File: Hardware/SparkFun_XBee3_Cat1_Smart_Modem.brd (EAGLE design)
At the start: 45.7 x 54.6 mm, 129 parts, among them J4 QWIIC_RIGHT_ANGLE, Q2 3.1A/30V/105mΩ, U1 FSUSB30MUX_MSOP10, U2 AP63203, U3 ESD Diode, U5 ESD Diode, U6 CP210X

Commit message: Updates xbee sybmol to include pin numbers
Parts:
- J2: device xbee_improved:XBEE-SMD_SILK -> xbee_smart_modem:XBEE-SMD_SILK
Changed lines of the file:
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@@
 <drawing>
 <settings>
-<setting alwaysvectorfont="no"/>
+<setting alwaysvectorfont="yes"/>
 <setting verticaltext="up"/>
 </settings>
@@
 <layers>
 <layer number="1" name="Top" color="4" fill="1" visible="yes" active="yes"/>
-<layer number="2" name="Route2" color="23" fill="1" visible="yes" active="yes"/>
-<layer number="15" name="Route15" color="39" fill="1" visible="yes" active="yes"/>
+<layer number="2" name="Route2" color="23" fill="1" visible="no" active="yes"/>
+<layer number="15" name="Route15" color="39" fill="1" visible="no" active="yes"/>
 <layer number="16" name="Bottom" color="3" fill="1" visible="yes" active="yes"/>
 <layer number="17" name="Pads" color="26" fill="1" visible="yes" active="yes"/>
@@
 <layer number="115" name="ReferenceISLANDS" color="7" fill="1" visible="no" active="yes"/>
 <layer number="116" name="Patch_BOT" color="9" fill="4" visible="no" active="yes"/>
-<layer number="117" name="PM_Ref" color="26" fill="1" visible="no" active="yes"/>
+<layer number="117" name="PM_Ref" color="26" fill="1" visible="yes" active="yes"/>
 <layer number="118" name="Rect_Pads" color="7" fill="1" visible="no" active="yes"/>
-<layer number="119" name="PF_Ref" color="31" fill="1" visible="no" active="yes"/>
-<layer number="120" name="WFL_Ref" color="25" fill="1" visible="no" active="yes"/>
+<layer number="119" name="PF_Ref" color="31" fill="1" visible="yes" active="yes"/>
+<layer number="120" name="WFL_Ref" color="25" fill="1" visible="yes" active="yes"/>
 <layer number="121" name="_tsilk" color="7" fill="1" visible="no" active="yes"/>
 <layer number="122" name="_bsilk" color="7" fill="1" visible="no" active="yes"/>
@@
 <attribute name="VALUE" x="33.02" y="7.62" size="0.6096" layer="27" font="vector" ratio="20" align="bottom-center"/>
 </element>
-<element name="J2" library="xbee_improved" package="XBEE-SMD_SILK" value="" x="22.86" y="33.02" smashed="yes">
+<element name="J2" library="xbee_smart_modem" package="XBEE-SMD_SILK" value="" x="22.86" y="33.02" smashed="yes">
 <attribute name="NAME" x="22.86" y="33.29" size="0.6096" layer="25" font="vector" ratio="20" align="bottom-center"/>
+<attribute name="PROD_ID" value="WRL-17581" x="22.86" y="33.02" size="1.778" layer="27" display="off"/>
 <attribute name="VALUE" x="22.86" y="32.75" size="0.6096" layer="27" font="vector" ratio="20" align="top-center"/>
 </element>
@@
 </signals>
 <mfgpreviewcolors>
-<mfgpreviewcolor name="soldermaskcolor" color="0xC8AA0000"/>
+<mfgpreviewcolor name="soldermaskcolor" color="0xC8000000"/>
 <mfgpreviewcolor name="silkscreencolor" color="0xFFFEFEFE"/>
 <mfgpreviewcolor name="backgroundcolor" color="0xFF282828"/>

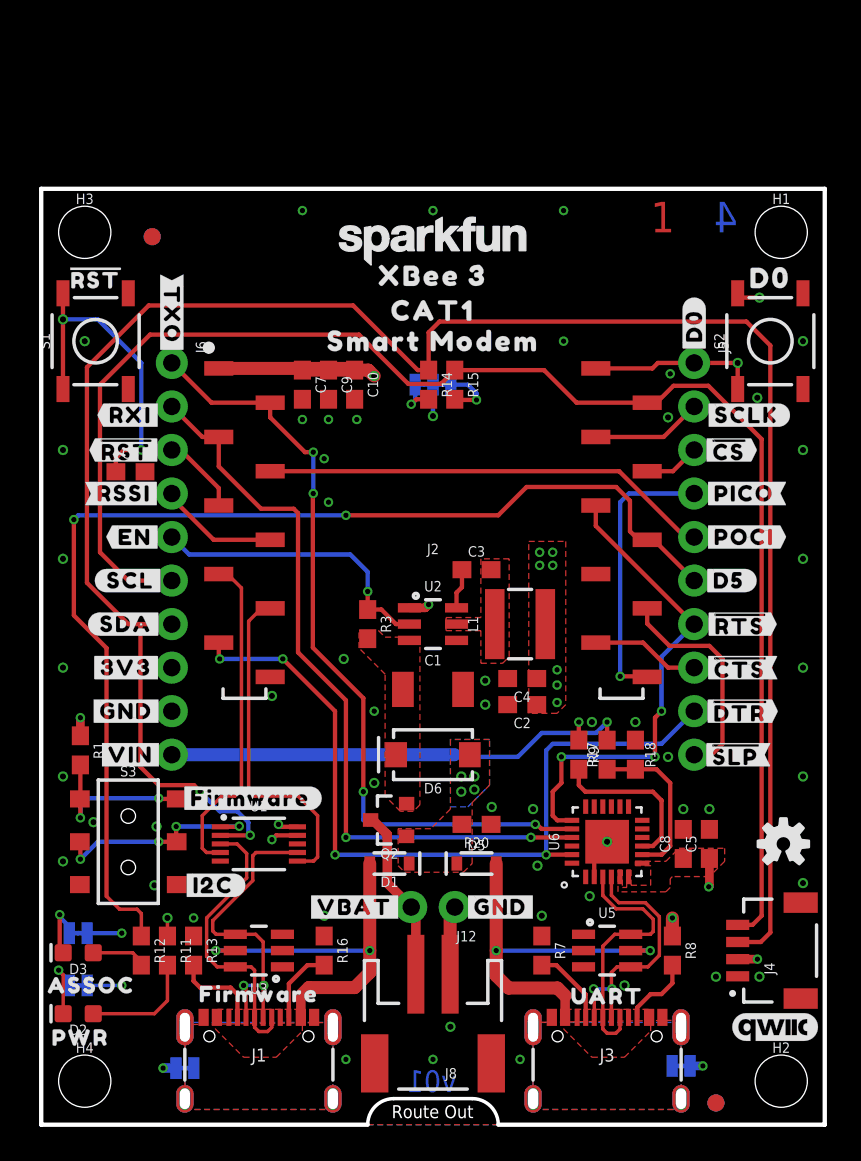
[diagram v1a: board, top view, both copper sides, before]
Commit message: Updates library to include a version of the module with silk
* Replaces module in design with the silk-ed version
* Extends board to be able to include the module's outline in silk
* Moves buttons and through holes to fit new size
* Changes name of the product to "Xbee 3 Dev Kit"
* Moves switch to make space for new silk
* Adds RSSI LED
* Rolls version to v02
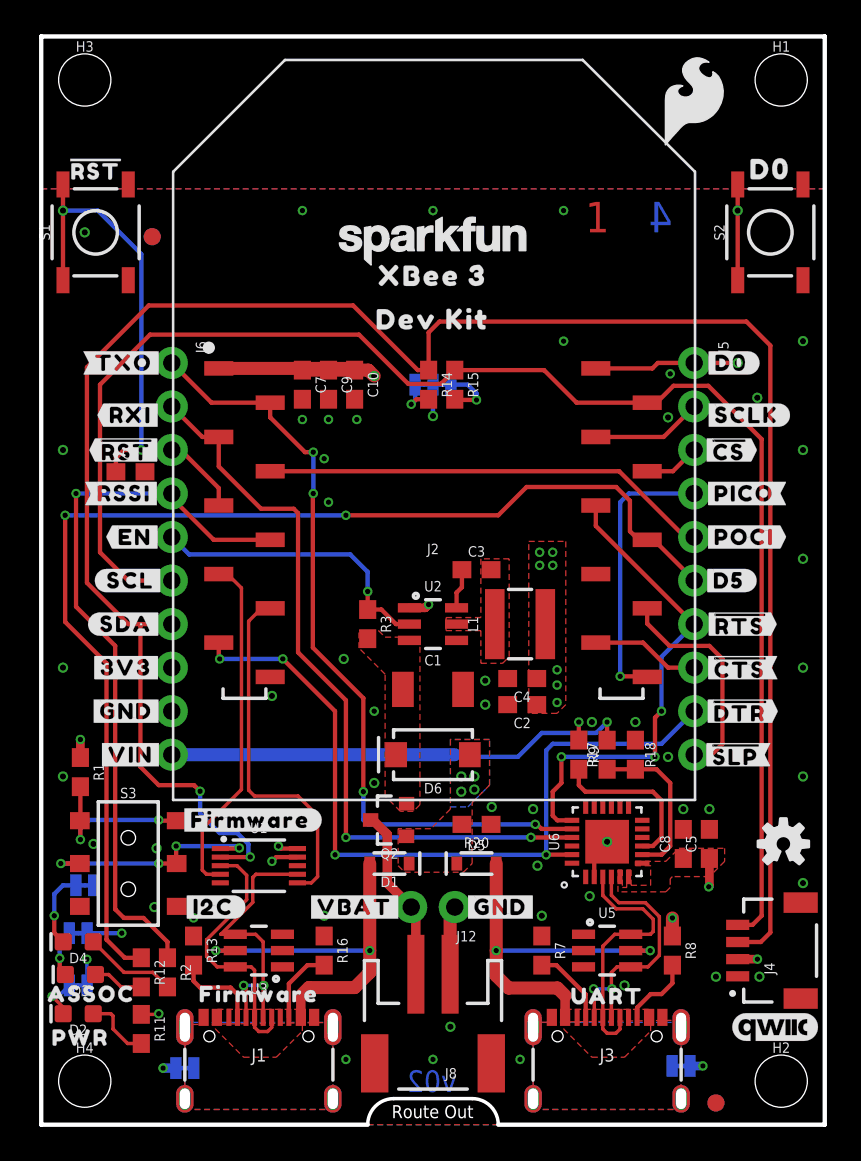
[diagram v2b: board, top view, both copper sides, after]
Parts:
- removed U$62: (no value), top:SMART1337
- removed U$64: (no value), top:MODEM1338
- added D4: BLUE, SparkFun-LED:LED-0603
- added R2: 2.2k, SparkFun-Resistors:0603
- added RLED: JUMPER-SMT_2_NC_TRACE_SILK, SparkFun-Jumpers:SMT-JUMPER_2_NC_TRACE_SILK
- J2: device xbee_smart_modem:XBEE-SMD_SILK -> xbee_smart_modem:XBEE3-SMD_SILK
- U$51: device top:SMART_MODEM1337 -> top:DEV_KIT1340
- U$52: device top:CAT1336 -> top:DEV_KIT1340
- U$61: device top:CAT1336 -> SparkFun-Aesthetics:SFE_LOGO_FLAME_.2
- moved U$61 27.5 mm to (38.1, 59.7), flipped to the top
- moved U$52 10.7 mm to (22.9, 36.8), flipped to the bottom
- moved H1 8.89 mm to (43.2, 61.0)
- moved H3 8.89 mm to (2.54, 61.0)
- moved S1 6.35 mm to (3.17, 52.1)
- moved S2 6.35 mm to (42.5, 52.1)
- moved U$30 6.35 mm to (3.17, 55.8)
- moved U$40 6.35 mm to (42.5, 55.8)
- moved R11 4.82 mm to (5.84, 5.59)
- moved U$50 3.95 mm to (4.83, 44.5), turned to 0 degrees
- moved U$10 3.05 mm to (40.3, 44.5), turned to 0 degrees
- moved D3 1.28 mm to (2.29, 8.76)
- moved U$51 1.27 mm to (22.9, 47.0)
- moved S3 1.27 mm to (5.08, 15.2)
- moved U$49 1.27 mm to (10.0, 12.7)
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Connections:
- net N$3 renamed FIRMWARE
- new net N$2: D4.A, R2.2
- new net N$3: D4.C, RLED.2
- net D10/RSSI_PWM: now also R2.1
- net GND: now also RLED.1
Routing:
- net D10/RSSI_PWM: track 7.01 -> 42.6 mm, vias 0 -> 1
- net D0: track 15.8 -> 22.9 mm
- net !RESET!: track 25.2 -> 31.6 mm
- net N$2: track 0.00 -> 5.42 mm
- net N$3: track 0.00 -> 4.48 mm, vias 0 -> 1
- net N$7: track 6.72 -> 3.97 mm
- net D5/ASSOCIATE: track 66.8 -> 68.9 mm
- net DIRECT_D-: track 18.8 -> 17.0 mm
- net D11/SDA: track 119.4 -> 120.7 mm
- net DIRECT_D+: track 17.0 -> 15.7 mm
- net N$23: track 3.80 -> 2.55 mm
- net XBEE_D-: track 19.8 -> 21.0 mm
- net DIRECT_SELECT: track 13.2 -> 14.1 mm
- net N$21: track 3.62 -> 2.78 mm
- net XBEE_D+/SDA: track 19.5 -> 20.3 mm
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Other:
- board size 45.7 x 54.6 mm -> 45.7 x 63.5 mm
- board text added: "v02"
- board text removed: "v01"

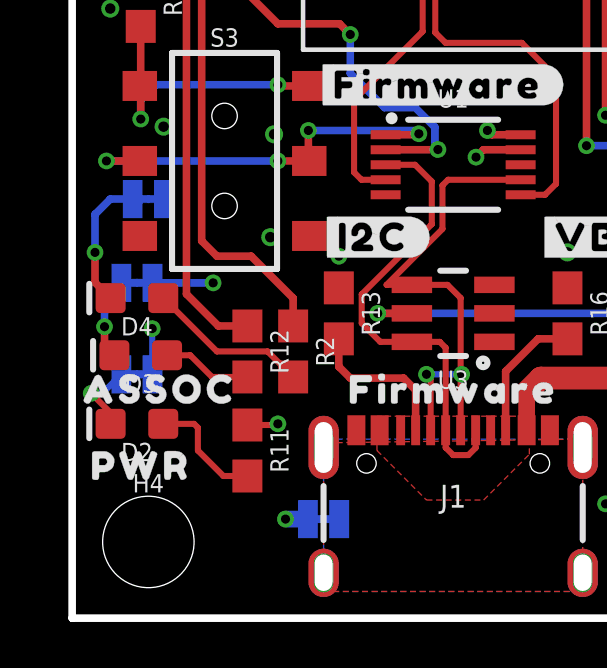
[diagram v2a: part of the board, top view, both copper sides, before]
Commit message: Adds silk to new LED and its' jumper
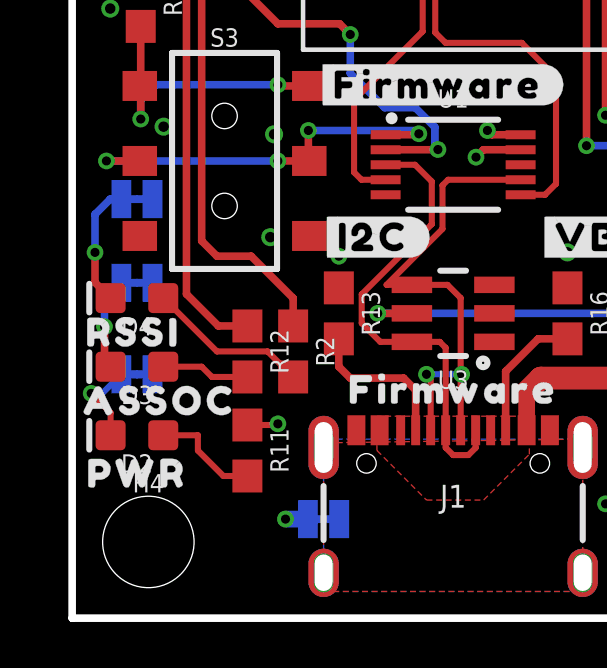
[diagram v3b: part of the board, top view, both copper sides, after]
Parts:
- added U$62: (no value), top:RSSI31
- added U$64: (no value), top:#RLED#22
- moved D3 0.40 mm to (2.16, 8.38)
- moved D2 0.38 mm to (2.16, 6.10)
- moved RLED 0.38 mm to (2.16, 14.0)
- moved U$43 0.38 mm to (2.92, 7.24)
- moved U$42 0.28 mm to (2.16, 4.83)
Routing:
- net GND: track 14.1 -> 10.6 mm, vias 57 -> 55
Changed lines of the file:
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@@
 <layer number="19" name="Unrouted" color="6" fill="1" visible="yes" active="yes"/>
 <layer number="20" name="Dimension" color="15" fill="1" visible="yes" active="yes"/>
-<layer number="21" name="tPlace" color="16" fill="1" visible="no" active="yes"/>
-<layer number="22" name="bPlace" color="14" fill="1" visible="no" active="yes"/>
+<layer number="21" name="tPlace" color="16" fill="1" visible="yes" active="yes"/>
+<layer number="22" name="bPlace" color="14" fill="1" visible="yes" active="yes"/>
 <layer number="23" name="tOrigins" color="15" fill="1" visible="yes" active="yes"/>
 <layer number="24" name="bOrigins" color="15" fill="1" visible="yes" active="yes"/>
@@
 <layer number="37" name="tTest" color="7" fill="1" visible="no" active="yes"/>
 <layer number="38" name="bTest" color="7" fill="1" visible="no" active="yes"/>
-<layer number="39" name="tKeepout" color="4" fill="11" visible="yes" active="yes"/>
+<layer number="39" name="tKeepout" color="4" fill="11" visible="no" active="yes"/>
 <layer number="40" name="bKeepout" color="1" fill="11" visible="no" active="yes"/>
 <layer number="41" name="tRestrict" color="4" fill="10" visible="no" active="yes"/>
@@
 <attribute name="VALUE" value="1k" x="5.08" y="5.588" size="0.6096" layer="27" font="vector" ratio="20" rot="R270" align="top-center"/>
 </element>
-<element name="D2" library="SparkFun-LED" package="LED-0603" value="RED" x="2.159" y="6.477" smashed="yes" rot="R180">
-<attribute name="NAME" x="2.159" y="5.842" size="0.6096" layer="25" font="vector" ratio="20" rot="R180" align="bottom-center"/>
-<attribute name="PROD_ID" value="DIO-00819" x="2.159" y="6.477" size="1.778" layer="27" rot="R180" display="off"/>
-<attribute name="VALUE" x="2.159" y="7.112" size="0.6096" layer="27" font="vector" ratio="20" rot="R180" align="top-center"/>
-</element>
-<element name="D3" library="SparkFun-LED" package="LED-0603" value="BLUE" x="2.286" y="8.763" smashed="yes" rot="R180">
-<attribute name="NAME" x="2.286" y="8.128" size="0.6096" layer="25" font="vector" ratio="20" rot="R180" align="bottom-center"/>
-<attribute name="PROD_ID" value="DIO-08575" x="2.286" y="8.763" size="1.778" layer="27" rot="R180" display="off"/>
-<attribute name="VALUE" x="2.286" y="9.398" size="0.6096" layer="27" font="vector" ratio="20" rot="R180" align="top-center"/>
+<element name="D2" library="SparkFun-LED" package="LED-0603" value="RED" x="2.159" y="6.096" smashed="yes" rot="R180">
+<attribute name="NAME" x="2.159" y="5.461" size="0.6096" layer="25" font="vector" ratio="20" rot="R180" align="bottom-center"/>
+<attribute name="PROD_ID" value="DIO-00819" x="2.159" y="6.096" size="1.778" layer="27" rot="R180" display="off"/>
+<attribute name="VALUE" x="2.159" y="6.731" size="0.6096" layer="27" font="vector" ratio="20" rot="R180" align="top-center"/>
+</element>
+<element name="D3" library="SparkFun-LED" package="LED-0603" value="BLUE" x="2.159" y="8.382" smashed="yes" rot="R180">
+<attribute name="NAME" x="2.159" y="7.747" size="0.6096" layer="25" font="vector" ratio="20" rot="R180" align="bottom-center"/>
+<attribute name="PROD_ID" value="DIO-08575" x="2.159" y="8.382" size="1.778" layer="27" rot="R180" display="off"/>
+<attribute name="VALUE" x="2.159" y="9.017" size="0.6096" layer="27" font="vector" ratio="20" rot="R180" align="top-center"/>
 </element>
 <element name="R12" library="SparkFun-Resistors" package="0603" value="2.2k" x="5.842" y="8.89" smashed="yes" rot="R270">
@@
 <element name="U$39" library="bot" package="#D5#3" value="" x="40.132" y="31.75" smashed="yes"/>
 <element name="U$41" library="top" package="#VIN#4" value="" x="5.207" y="21.59" smashed="yes"/>
-<element name="U$42" library="top" package="PWR26" value="" x="2.286" y="5.08" smashed="yes"/>
-<element name="U$43" library="top" package="ASSOC27" value="" x="2.921" y="7.62" smashed="yes"/>
+<element name="U$42" library="top" package="PWR26" value="" x="2.159" y="4.826" smashed="yes"/>
+<element name="U$43" library="top" package="ASSOC27" value="" x="2.921" y="7.239" smashed="yes"/>
 <element name="U$44" library="top" package="#3V3#1" value="" x="10.287" y="26.67" smashed="yes" rot="MR0"/>
 <element name="U$45" library="top" package="#GND#0" value="" x="10.287" y="24.13" smashed="yes" rot="MR0"/>
@@
 <attribute name="VALUE" x="6.604" y="8.89" size="0.6096" layer="27" font="vector" ratio="20" rot="R270" align="top-center"/>
 </element>
-<element name="RLED" library="SparkFun-Jumpers" package="SMT-JUMPER_2_NC_TRACE_SILK" package3d_urn="urn:adsk.eagle:package:39281/1" value="JUMPER-SMT_2_NC_TRACE_SILK" x="2.54" y="13.97" smashed="yes" rot="MR0">
-<attribute name="NAME" x="2.54" y="15.113" size="0.6096" layer="26" font="vector" ratio="20" rot="MR0" align="bottom-center"/>
-<attribute name="VALUE" x="2.54" y="12.827" size="0.6096" layer="28" font="vector" ratio="20" rot="MR0" align="top-center"/>
-</element>
+<element name="RLED" library="SparkFun-Jumpers" package="SMT-JUMPER_2_NC_TRACE_SILK" package3d_urn="urn:adsk.eagle:package:39281/1" value="JUMPER-SMT_2_NC_TRACE_SILK" x="2.159" y="13.97" smashed="yes" rot="MR0">
+<attribute name="NAME" x="2.159" y="15.113" size="0.6096" layer="26" font="vector" ratio="20" rot="MR0" align="bottom-center"/>
+<attribute name="VALUE" x="2.159" y="12.827" size="0.6096" layer="28" font="vector" ratio="20" rot="MR0" align="top-center"/>
+</element>
+<element name="U$62" library="top" package="RSSI31" value="" x="2.032" y="9.525" smashed="yes"/>
+<element name="U$64" library="top" package="#RLED#22" value="" x="5.588" y="13.97" smashed="yes" rot="MR0"/>
 </elements>
 <signals>
@@
 <wire x1="38.608" y1="3.429" x2="37.8587" y2="3.429" width="0.508" layer="16"/>
 <via x="38.608" y="3.429" extent="1-16" drill="0.3048"/>
-<wire x1="2.6797" y1="11.176" x2="4.699" y2="11.176" width="0.254" layer="16"/>
-<via x="4.699" y="11.176" extent="1-16" drill="0.3048"/>
 <via x="7.112" y="3.302" extent="1-16" drill="0.3048"/>
 <via x="19.431" y="24.13" extent="1-16" drill="0.3048"/>
@@
 <via x="8.89" y="12.065" extent="1-16" drill="0.3048"/>
 <wire x1="2.6797" y1="8.128" x2="2.667" y2="8.1407" width="0.2032" layer="16"/>
-<wire x1="2.667" y1="9.652" x2="2.667" y2="8.1407" width="0.2032" layer="16"/>
-<via x="2.667" y="9.652" extent="1-16" drill="0.3048"/>
 <polygon width="0.254" layer="2" isolate="0.127" rank="3">
 <vertex x="0" y="0"/>
@@
 <contactref element="D2" pad="A"/>
 <wire x1="5.842" y1="4.738" x2="5.041" y2="4.738" width="0.2032" layer="1"/>
-<wire x1="4.191" y1="5.588" x2="4.191" y2="6.35" width="0.2032" layer="1"/>
-<wire x1="4.191" y1="6.35" x2="4.064" y2="6.477" width="0.2032" layer="1"/>
-<wire x1="4.064" y1="6.477" x2="3.036" y2="6.477" width="0.2032" layer="1"/>
+<wire x1="4.191" y1="5.588" x2="4.191" y2="6.096" width="0.2032" layer="1"/>
+<wire x1="4.191" y1="6.096" x2="3.036" y2="6.096" width="0.2032" layer="1"/>
 <wire x1="5.041" y1="4.738" x2="4.191" y2="5.588" width="0.2032" layer="1"/>
 </signal>
@@
 <contactref element="R12" pad="2"/>
 <contactref element="D3" pad="A"/>
-<wire x1="3.937" y1="8.763" x2="3.163" y2="8.763" width="0.2032" layer="1"/>
+<wire x1="4.318" y1="8.382" x2="3.036" y2="8.382" width="0.2032" layer="1"/>
 <wire x1="5.842" y1="8.04" x2="4.66" y2="8.04" width="0.2032" layer="1"/>
-<wire x1="4.66" y1="8.04" x2="3.937" y2="8.763" width="0.2032" layer="1"/>
+<wire x1="4.66" y1="8.04" x2="4.318" y2="8.382" width="0.2032" layer="1"/>
 </signal>
 <signal name="XBEE_D+/SDA" class="2">
@@
 <contactref element="ALED" pad="2"/>
 <contactref element="D3" pad="C"/>
-<wire x1="1.0795" y1="9.7155" x2="1.0795" y2="9.0925" width="0.254" layer="1"/>
-<wire x1="1.409" y1="8.763" x2="1.0795" y2="9.0925" width="0.254" layer="1"/>
+<wire x1="1.0795" y1="9.7155" x2="1.0795" y2="8.5845" width="0.254" layer="1"/>
+<wire x1="1.282" y1="8.382" x2="1.0795" y2="8.5845" width="0.254" layer="1"/>
 <via x="1.0795" y="9.7155" extent="1-16" drill="0.3048"/>
-<wire x1="1.6383" y1="11.176" x2="1.58115" y2="11.11885" width="0.254" layer="16"/>
-<wire x1="1.58115" y1="11.11885" x2="1.0795" y2="10.6172" width="0.254" layer="16"/>
+<wire x1="1.6383" y1="11.176" x2="1.0795" y2="10.6172" width="0.254" layer="16"/>
 <wire x1="1.0795" y1="10.6172" x2="1.0795" y2="9.7155" width="0.254" layer="16"/>
 </signal>
@@
 <contactref element="PLED" pad="2"/>
 <contactref element="D2" pad="C"/>
-<wire x1="1.282" y1="6.477" x2="1.282" y2="6.846" width="0.2032" layer="1"/>
+<wire x1="1.282" y1="6.096" x2="1.282" y2="6.846" width="0.2032" layer="1"/>
 <wire x1="1.282" y1="6.846" x2="0.635" y2="7.493" width="0.2032" layer="1"/>
 <via x="0.635" y="7.493" extent="1-16" drill="0.3048"/>
@@
 <wire x1="0.762" y1="11.188" x2="0.762" y2="12.192" width="0.254" layer="1"/>
 <via x="0.762" y="12.192" extent="1-16" drill="0.3048"/>
-<wire x1="2.0193" y1="13.97" x2="1.27" y2="13.97" width="0.254" layer="16"/>
+<wire x1="1.6383" y1="13.97" x2="1.27" y2="13.97" width="0.254" layer="16"/>
 <wire x1="1.27" y1="13.97" x2="0.762" y2="13.462" width="0.254" layer="16"/>
 <wire x1="0.762" y1="13.462" x2="0.762" y2="12.192" width="0.254" layer="16"/>
